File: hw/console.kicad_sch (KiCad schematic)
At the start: 44 parts, among them J1 Debug Port, Q4 AP2301, Q5 AP2302, Q6 AP2301, Q7 AP2302, SW2 SW_Push, SW3 SW_Push, SW4 SW_Push, SW5 SW_Push, SW6 SW_Push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

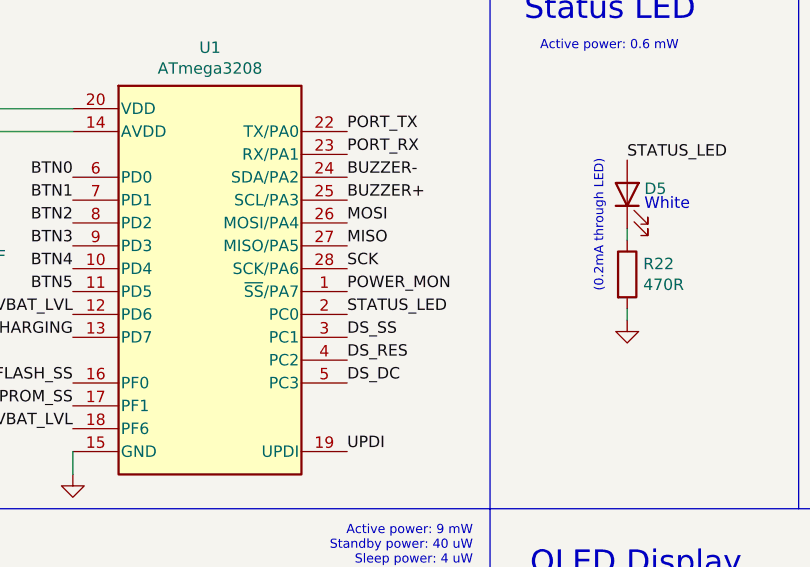
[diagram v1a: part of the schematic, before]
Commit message: PCB: removed power monitor
Far from enough capacity on board to ever be useful.
Power monitor was envisioned to prevent EEPROM corruption. This was instead prevented with atomic operation (copy before write).
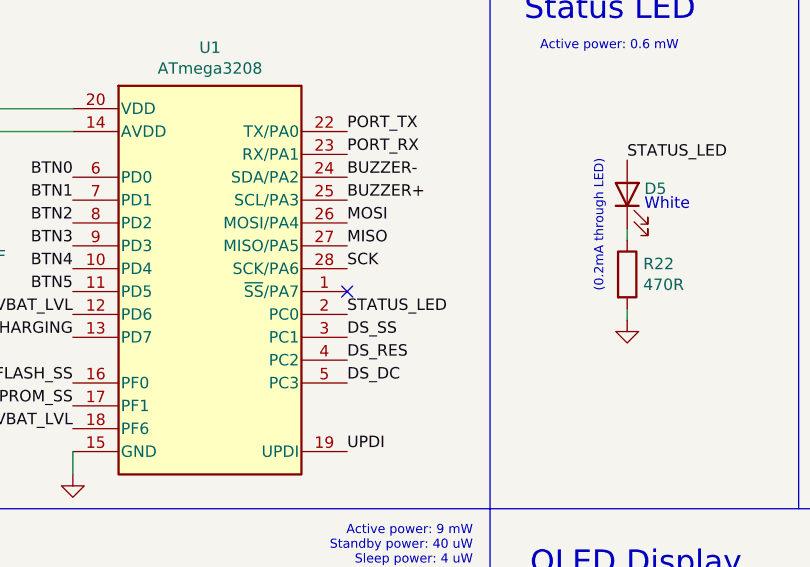
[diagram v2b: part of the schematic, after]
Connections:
- net POWER_MON: no longer U1.1 (~{SS}/PA7)
- no-connect marks 2 -> 3
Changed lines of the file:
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@@
     (title "Handheld game console")
     (date "2021-11-16")
-    (rev "2021B")
+    (rev "2022A")
   )
   (junction (at 222.25 41.91) (diameter 0) (color 0 0 0 0)
@@
   (no_connect (at 158.75 117.475))
   (no_connect (at 51.435 172.085))
+  (no_connect (at 82.55 49.53))
   (wire (pts (xy 227.33 39.37) (xy 227.33 41.91))
     (stroke (width 0) (type default) (color 0 0 0 0))
@@
   )
   (label "DS_SS" (at 82.55 54.61 0)
-    (effects (font (size 1.27 1.27)) (justify left bottom))
-  )
-  (label "POWER_MON" (at 82.55 49.53 0)
     (effects (font (size 1.27 1.27)) (justify left bottom))
   )
@@
       (reference "#PWR01") (unit 1) (value "+2.8V") (footprint "")
     )
-    (path "/00000000-0000-0000-0000-00006188ce03/00000000-0000-0000-0000-0000619e49b2"
-      (reference "#PWR02") (unit 1) (value "VBAT") (footprint "")
-    )
-    (path "/00000000-0000-0000-0000-00006188ce03/00000000-0000-0000-0000-0000619f1728"
-      (reference "#PWR03") (unit 1) (value "+2.8V") (footprint "")
-    )
-    (path "/00000000-0000-0000-0000-00006188ce03/00000000-0000-0000-0000-0000619e9629"
-      (reference "#PWR04") (unit 1) (value "GND") (footprint "")
-    )
     (path "/00000000-0000-0000-0000-000061a109a7"
       (reference "#PWR05") (unit 1) (value "GND") (footprint "")
@@
       (reference "Q7") (unit 1) (value "AP2302") (footprint "Package_TO_SOT_SMD:SOT-23")
     )
-    (path "/00000000-0000-0000-0000-00006188ce03/00000000-0000-0000-0000-000061a67816"
-      (reference "Q8") (unit 1) (value "AP2301") (footprint "Package_TO_SOT_SMD:SOT-23")
-    )
     (path "/00000000-0000-0000-0000-00006188ce03/00000000-0000-0000-0000-0000618c396b"
       (reference "R1") (unit 1) (value "330k") (footprint "Resistor_SMD:R_0603_1608Metric")
@@
       (reference "R22") (unit 1) (value "470R") (footprint "Resistor_SMD:R_0603_1608Metric")
     )
-    (path "/00000000-0000-0000-0000-00006188ce03/00000000-0000-0000-0000-0000619dc5d0"
-      (reference "R23") (unit 1) (value "100k") (footprint "Resistor_SMD:R_0603_1608Metric")
-    )
     (path "/00000000-0000-0000-0000-000061c06cd0"
